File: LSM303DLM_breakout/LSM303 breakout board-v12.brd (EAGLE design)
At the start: 21.6 x 20.3 mm, 20 parts, among them Q1 MOSFET-N-CH, Q2 MOSFET-N-CH, U1 LSM303DLHSMD, U2 1.8V, U3 3.3V

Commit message: Finished?
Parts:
- moved C7 2.65 mm to (5.84, 7.37), turned to 180 degrees
- moved SJ1 2.09 mm to (8.89, 4.32)
- moved U2 1.93 mm to (5.84, 9.40), turned to 270 degrees
- moved C1 1.78 mm to (17.8, 13.0)
- moved C3 1.78 mm to (15.0, 13.7)
- moved C4 1.78 mm to (15.0, 12.2)
- moved C2 1.78 mm to (17.8, 9.40)
- moved C6 1.78 mm to (17.8, 7.87)
- moved C8 1.78 mm to (17.8, 6.35), turned to 180 degrees
- moved U3 0.92 mm to (15.5, 3.56), turned to 270 degrees
- moved Q1 0.76 mm to (8.89, 17.8)
- moved Q2 0.76 mm to (8.89, 14.0)
- moved R1 0.76 mm to (12.2, 17.8)
- moved R2 0.76 mm to (12.2, 14.0)
- moved U1 0.76 mm to (11.9, 8.38)
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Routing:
- net 1.8V: track 23.6 -> 17.3 mm
- net N$7: track 1.43 -> 4.89 mm
- net SA0_A: track 2.38 -> 4.51 mm
- net N$12: track 3.94 -> 1.82 mm
- net N$11: track 7.72 -> 5.83 mm
- net 3.3V: track 13.5 -> 15.3 mm
- net N$10: track 5.70 -> 3.93 mm
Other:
- board size 21.6 x 20.3 mm -> 20.3 x 20.3 mm

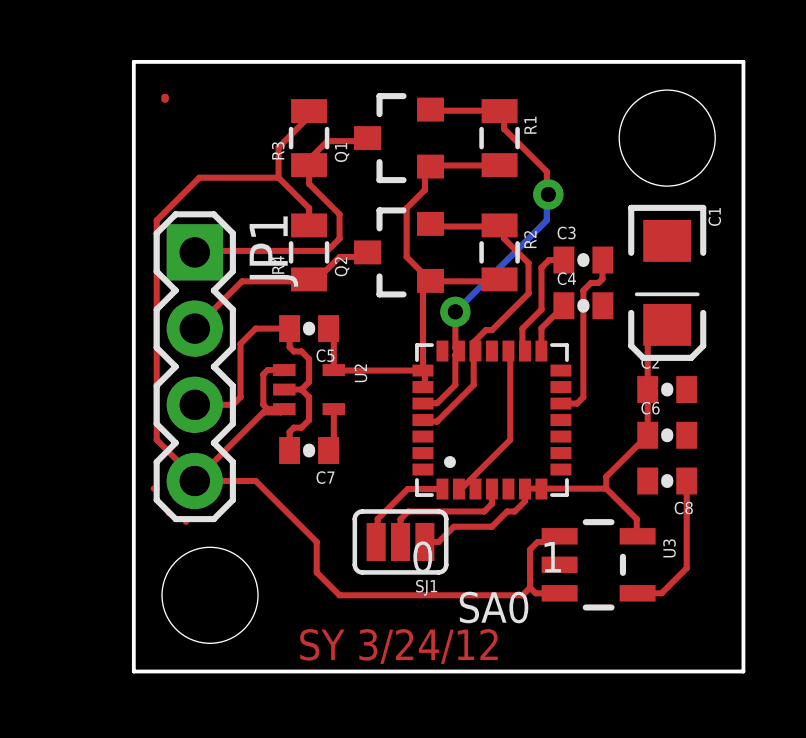
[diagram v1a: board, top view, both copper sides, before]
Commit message: Make traces thicker.
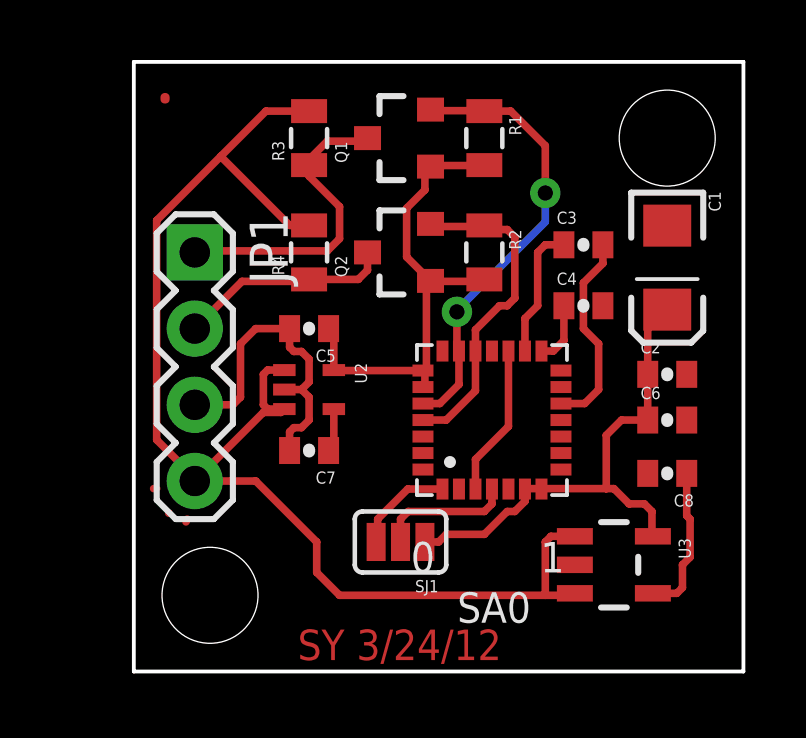
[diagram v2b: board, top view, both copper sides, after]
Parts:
- moved C2 0.51 mm to (17.8, 9.91)
- moved C3 0.51 mm to (15.0, 14.2)
- moved R1 0.51 mm to (11.7, 17.8)
- moved R2 0.51 mm to (11.7, 14.0)
- moved C6 0.51 mm to (17.8, 8.38)
- moved C1 0.51 mm to (17.8, 13.5)
- moved U3 0.51 mm to (16.0, 3.56)
- moved C8 0.25 mm to (17.8, 6.60)
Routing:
- net VCC: track 42.2 -> 44.1 mm
- net 3.3V: track 15.3 -> 17.0 mm
- net 1.8V: track 17.3 -> 16.3 mm
- net N$11: track 5.83 -> 6.75 mm
- net N$10: track 3.93 -> 4.44 mm

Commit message: Version 0.1.
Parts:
- moved SJ1 1.37 mm to (7.62, 3.81)
- moved U3 0.51 mm to (16.5, 3.56)
- moved C5 0.51 mm to (6.35, 11.4)
- moved C7 0.51 mm to (6.35, 7.37)
- moved R3 0.25 mm to (5.59, 17.8)
- moved R4 0.25 mm to (5.59, 14.0)
- moved U2 0.25 mm to (5.59, 9.40)
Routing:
- net GND: track 20.1 -> 5.44 mm
- net 3.3V: track 17.0 -> 19.7 mm
- net SA0_A: track 4.51 -> 6.14 mm
- net VCC: track 44.1 -> 44.8 mm
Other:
- board text added: "SY 3/26/12"
- board text removed: "SY 3/24/12"

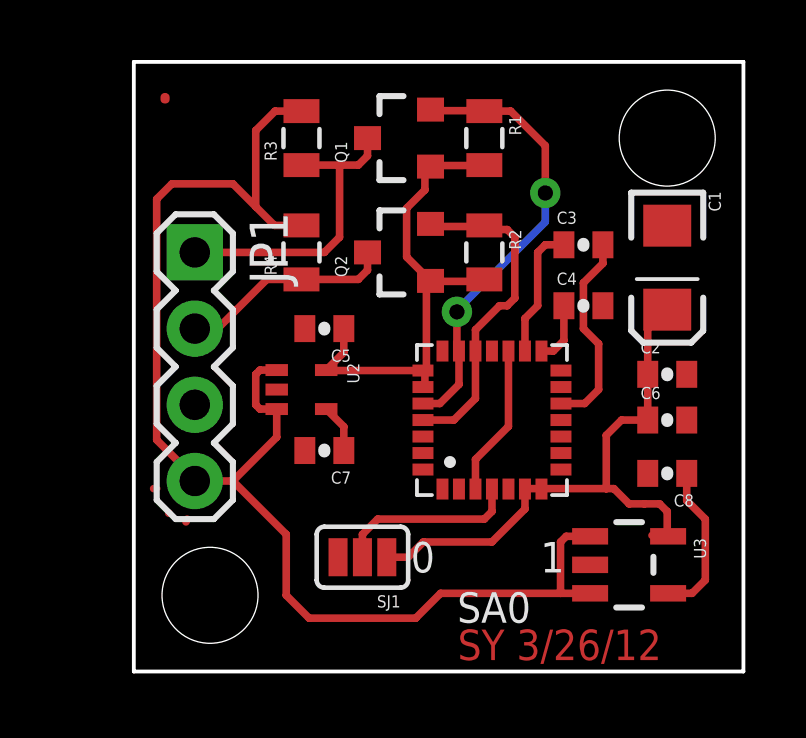
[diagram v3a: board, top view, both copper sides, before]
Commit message: Version 0.2. Make board a lot simpler.
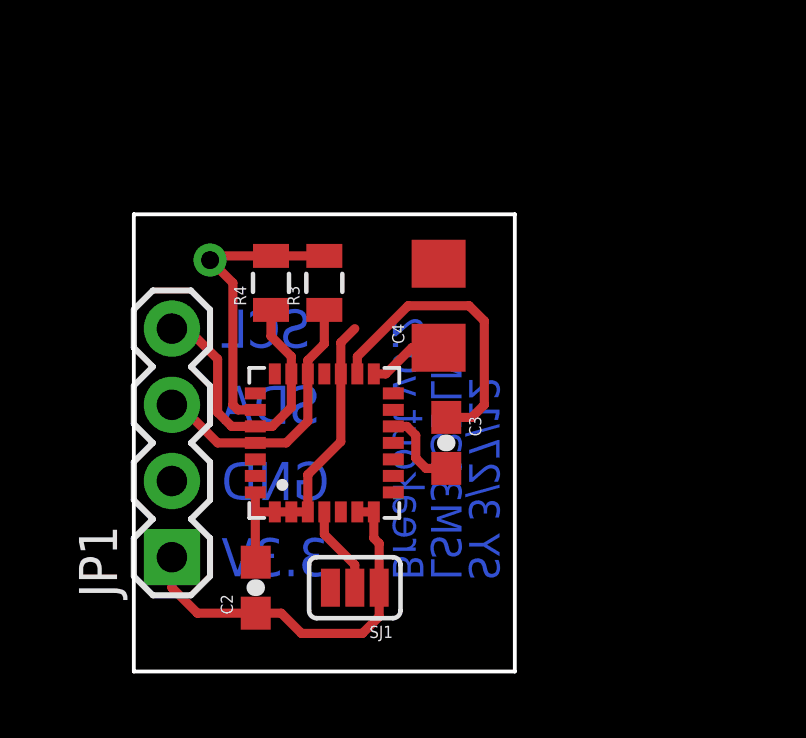
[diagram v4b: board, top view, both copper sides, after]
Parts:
- removed C1: 10uF, SparkFun:EIA3216
- removed C5, C6: 2.2uF, SparkFun:0402-CAP
- removed C7, C8: 470pF, SparkFun:0402-CAP
- removed Q1, Q2: MOSFET-N-CH, SparkFun:SOT23-3
- removed R1, R2: 4.7k, SparkFun:0805
- removed U2: 1.8V, SparkFun:SC70
- removed U3: 3.3V, SparkFun:SOT23-5
- C2, C3: device SparkFun:0402-CAP -> SparkFun:0603-CAP
- C4: device SparkFun:0402-CAP -> SparkFun:1206
- JP1: device SparkFun:1X04 -> SparkFun-Connectors:1X04
- moved C2 15.5 mm to (4.06, 2.79), turned to 90 degrees
- moved JP1 10.2 mm to (1.27, 3.81), turned to 90 degrees
- moved C3 8.03 mm to (10.4, 7.62), turned to 270 degrees
- moved U1 5.64 mm to (6.35, 7.62)
- moved R3 4.89 mm to (6.35, 13.0)
- moved C4 4.83 mm to (10.2, 12.2), turned to 90 degrees
- moved R4 1.44 mm to (4.57, 13.0)
- moved SJ1 1.05 mm to (7.37, 2.79)
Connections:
- removed net 1.8V: C5.1, Q1.1, Q2.1, R1.2, R2.2, U1.22, U1.23, U2.5
- removed net GND: C1.C, C2.2, C4.2, C5.2, C6.2, C7.2, C8.2, JP1.3, SJ1.3, U1.1, U1.17, U1.2, U1.28, U1.3, U2.2, U3.2
- removed net N$6: C7.1, U2.4
- removed net N$7: C8.1, U3.4
- removed net SCL_M: Q1.2, R1.1, U1.20, U1.24
- removed net SDA_M: Q2.2, R2.1, U1.19, U1.25
- removed net VCC: JP1.4, R3.2, R4.2, U2.1, U2.3, U3.1, U3.3
- new net N$1: C2.2, C4.2, JP1.2, SJ1.3, U1.1, U1.17, U1.2, U1.28, U1.3
- net 3.3V: now also JP1.1, R3.2, R4.2, U1.23; no longer C1.A, C6.1, U3.5
- net SCL: now also JP1.4, R4.1, U1.20, U1.24; no longer JP1.1, Q1.3, R3.1
- net SDA: now also JP1.3, R3.1, U1.19, U1.25; no longer JP1.2, Q2.3, R4.1
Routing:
- net VCC: track 44.8 -> 0.00 mm
- net 1.8V: track 16.7 -> 0.00 mm
- net SCL_M: track 15.2 -> 0.00 mm, vias 2 -> 0
- net SDA_M: track 11.2 -> 0.00 mm
- net N$1: track 0.00 -> 11.2 mm
- net N$10: track 4.44 -> 9.96 mm
- net GND: track 5.44 -> 0.00 mm
- net N$7: track 5.24 -> 0.00 mm
- net N$11: track 6.75 -> 2.79 mm
- net SA0_A: track 6.14 -> 2.95 mm
- net 3.3V: track 19.7 -> 22.7 mm, vias 0 -> 1
- net SDA: track 7.16 -> 9.30 mm
- net N$6: track 1.63 -> 0.00 mm
- added copper zone on layer 16, net 3.3V
- added copper zone on layer 1, net N$1
- removed copper zone on layer 1, net GND
- removed copper zone on layer 16, net GND
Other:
- board size 20.3 x 20.3 mm -> 12.7 x 15.2 mm
- board text added: "3.3V"
- board text added: "Breakout v0.2"
- board text added: "SY 3/27/12"
- board text removed: "0"
- board text removed: "1"
- board text removed: "Breakout"
- board text removed: "SA0"
- board text removed: "SY 3/26/12"
- board text removed: "Vin"

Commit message: Minor modifications.
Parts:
- R3, R4: device SparkFun:0805 -> SparkFun:0603-RES
- moved C3 0.72 mm to (10.9, 7.11)
- moved C2 0.25 mm to (4.32, 2.79)
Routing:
- net N$1: track 11.2 -> 12.6 mm
- net N$11: track 2.79 -> 3.81 mm
